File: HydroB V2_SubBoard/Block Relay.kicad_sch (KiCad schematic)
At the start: 25 parts, among them J14 Screw_Terminal_01x02, J15 Screw_Terminal_01x02, J16 Screw_Terminal_01x02, J17 Screw_Terminal_01x02, J18 Screw_Terminal_01x02, K10 SRD-05VDC-SL-C, K5 SRD-05VDC-SL-C, K7 SRD-05VDC-SL-C, K8 SRD-05VDC-SL-C, K9 SRD-05VDC-SL-C, Q10 S8050, Q6 S8050, Q7 S8050, Q8 S8050, Q9 S8050

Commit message: finish the subboard layout
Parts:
- J14, J15, J16, J17, J18: footprint Connector_Phoenix_MC:PhoenixContact_MC_1,5_2-G-3.5_1x02_P3.50mm_Horizontal -> Connector_Phoenix_MC:PhoenixContact_MC_1,5_2-G-3.81_1x02_P3.81mm_Horizontal
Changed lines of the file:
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@@
 			)
 		)
-		(property "Footprint" "Connector_Phoenix_MC:PhoenixContact_MC_1,5_2-G-3.5_1x02_P3.50mm_Horizontal"
+		(property "Footprint" "Connector_Phoenix_MC:PhoenixContact_MC_1,5_2-G-3.81_1x02_P3.81mm_Horizontal"
 			(at 172.72 58.42 0)
 			(effects
@@
 			)
 		)
-		(property "Footprint" "Connector_Phoenix_MC:PhoenixContact_MC_1,5_2-G-3.5_1x02_P3.50mm_Horizontal"
+		(property "Footprint" "Connector_Phoenix_MC:PhoenixContact_MC_1,5_2-G-3.81_1x02_P3.81mm_Horizontal"
 			(at 236.22 58.42 0)
 			(effects
@@
 			)
 		)
-		(property "Footprint" "Connector_Phoenix_MC:PhoenixContact_MC_1,5_2-G-3.5_1x02_P3.50mm_Horizontal"
+		(property "Footprint" "Connector_Phoenix_MC:PhoenixContact_MC_1,5_2-G-3.81_1x02_P3.81mm_Horizontal"
 			(at 101.6 58.42 0)
 			(effects
@@
 			)
 		)
-		(property "Footprint" "Connector_Phoenix_MC:PhoenixContact_MC_1,5_2-G-3.5_1x02_P3.50mm_Horizontal"
+		(property "Footprint" "Connector_Phoenix_MC:PhoenixContact_MC_1,5_2-G-3.81_1x02_P3.81mm_Horizontal"
 			(at 129.54 111.76 0)
 			(effects
@@
 			)
 		)
-		(property "Footprint" "Connector_Phoenix_MC:PhoenixContact_MC_1,5_2-G-3.5_1x02_P3.50mm_Horizontal"
+		(property "Footprint" "Connector_Phoenix_MC:PhoenixContact_MC_1,5_2-G-3.81_1x02_P3.81mm_Horizontal"
 			(at 215.9 111.76 0)
 			(effects

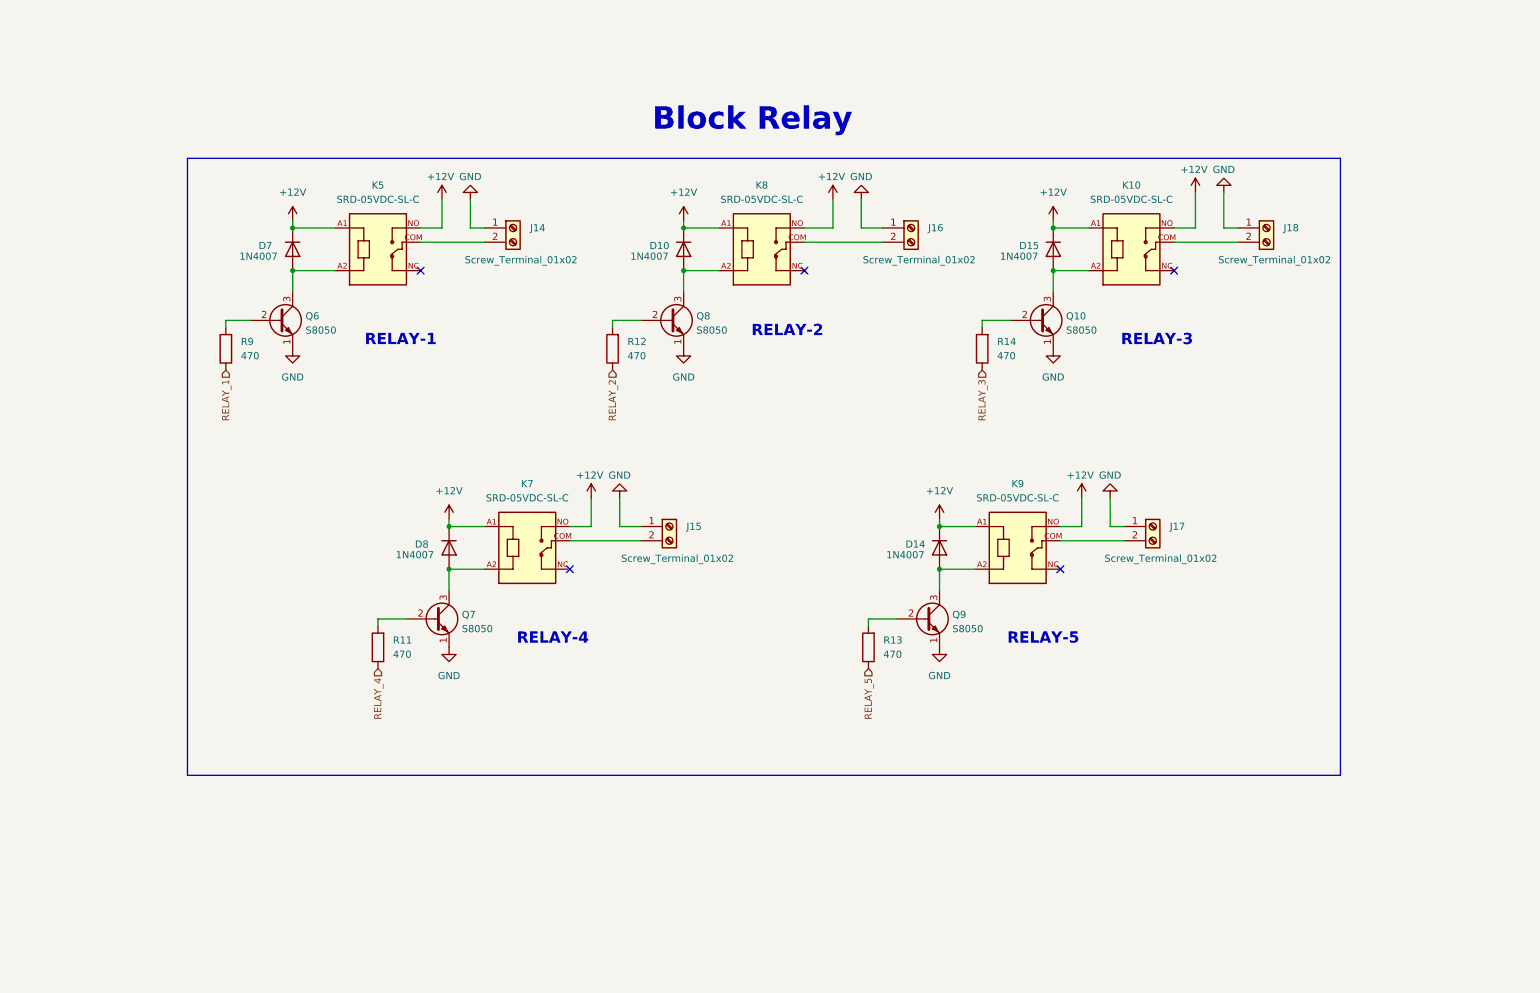
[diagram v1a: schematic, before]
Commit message: subboard updated for PCB placement
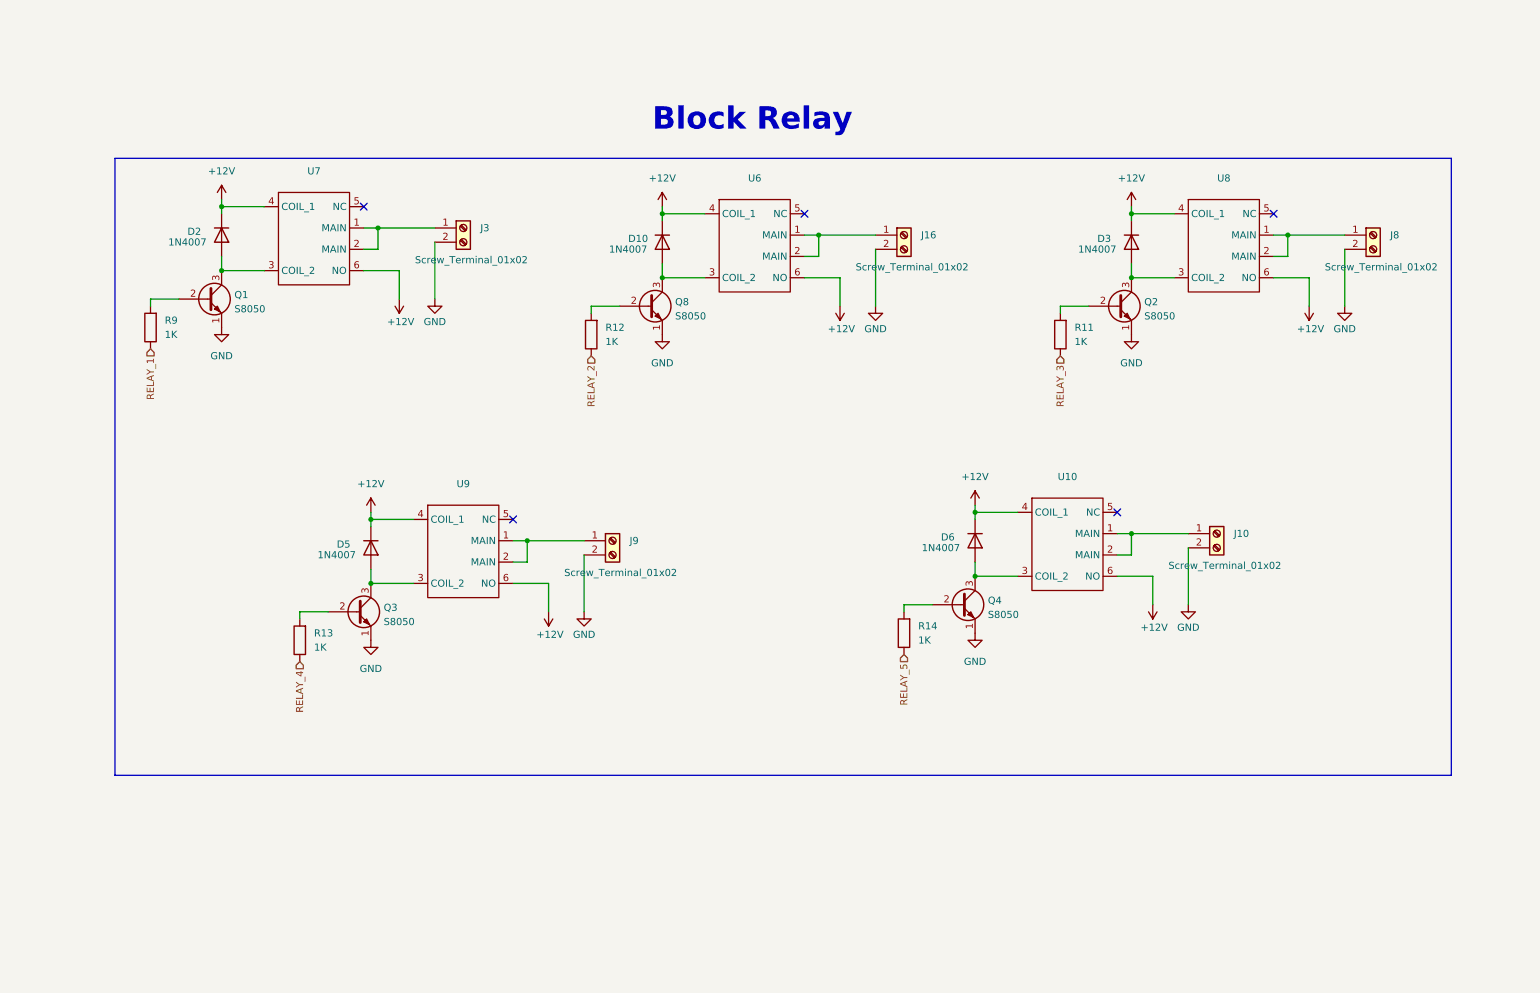
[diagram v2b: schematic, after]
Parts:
- removed D14, D15, D7, D8: 1N4007, Diode_SMD:D_SMA, symbol Diode:LL4148
- removed J14, J15, J17, J18: Screw_Terminal_01x02, Connector_Phoenix_MC:PhoenixContact_MC_1,5_2-G-3.81_1x02_P3.81mm_Horizontal, symbol Connector:Screw_Terminal_01x02
- removed K10, K5, K7, K8, K9: SRD-05VDC-SL-C, SRD-05VDC-SL-C (1):RELAY_SRD-05VDC-SL-C, symbol SRD-05VDC-SL-C:SRD-05VDC-SL-C
- removed Q10, Q6, Q7, Q9: S8050, Package_TO_SOT_SMD:SOT-23, symbol Transistor_BJT:S8050
- added D2, D3, D5, D6: 1N4007, Diode_SMD:D_SMA, symbol Diode:LL4148
- added J10, J3, J8, J9: Screw_Terminal_01x02, TerminalBlock_Phoenix:TerminalBlock_Phoenix_MKDS-1,5-2_1x02_P5.00mm_Horizontal, symbol Connector:Screw_Terminal_01x02
- added Q1, Q2, Q3, Q4: S8050, Package_TO_SOT_SMD:SOT-23, symbol Transistor_BJT:S8050
- added U10, U6, U7, U8, U9: ~, relay 12vdc 3A:RELAY-TH_SRS-12VDC-SL, symbol RELAY-12V-3A:RELAY-12V-3A
- J16: footprint Connector_Phoenix_MC:PhoenixContact_MC_1,5_2-G-3.81_1x02_P3.81mm_Horizontal -> TerminalBlock_Phoenix:TerminalBlock_Phoenix_MKDS-1,5-2_1x02_P5.00mm_Horizontal
- R11, R12, R13, R14, R9: value 470 -> 1K
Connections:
- net +12V: now also D2.1 (K), D3.1 (K), D5.1 (K), D6.1 (K), U10.4 (COIL_1), U10.6 (NO), U6.4 (COIL_1), U6.6 (NO), U7.4 (COIL_1), U7.6 (NO), U8.4 (COIL_1), U8.6 (NO), U9.4 (COIL_1), U9.6 (NO)
- net GND: now also J16.2 (Pin_2), J10.2 (Pin_2), J3.2 (Pin_2), J8.2 (Pin_2), J9.2 (Pin_2), Q1.1 (E), Q2.1 (E), Q3.1 (E), Q4.1 (E); no longer J16.1 (Pin_1)
- net RELAY_3: now also R11.1; no longer R14.1
- net RELAY_4: now also R13.1; no longer R11.1
- net RELAY_5: now also R14.1; no longer R13.1
- net at R11.2: now also Q2.2 (B)
- net at R14.2: now also Q4.2 (B)
- net at R13.2: now also Q3.2 (B)
- net at R9.2: now also Q1.2 (B)
- net at D10.2 (A), Q8.3 (C): now also U6.3 (COIL_2)
- new net: D6.2 (A), Q4.3 (C), U10.3 (COIL_2)
- new net: D3.2 (A), Q2.3 (C), U8.3 (COIL_2)
- new net: J10.1 (Pin_1), U10.1 (MAIN), U10.2 (MAIN)
- new net: J8.1 (Pin_1), U8.1 (MAIN), U8.2 (MAIN)
- new net: D5.2 (A), Q3.3 (C), U9.3 (COIL_2)
- new net: J16.1 (Pin_1), U6.1 (MAIN), U6.2 (MAIN)
- new net: D2.2 (A), Q1.3 (C), U7.3 (COIL_2)
- new net: J9.1 (Pin_1), U9.1 (MAIN), U9.2 (MAIN)
- new net: J3.1 (Pin_1), U7.1 (MAIN), U7.2 (MAIN)
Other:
- note removed: "RELAY-1"
- note removed: "RELAY-2"
- note removed: "RELAY-3"
- note removed: "RELAY-4"
- note removed: "RELAY-5"
- moved on the sheet: D10, J16, Q8, R12

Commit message: Subboard updated
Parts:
- added R18, R2, R22, R23, R3: 10K, Resistor_SMD:R_0603_1608Metric, symbol Device:R
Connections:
- net GND: now also R18.1, R2.1, R22.1, R23.1, R3.1
- net at Q4.2 (B), R14.2: now also R23.2
- net at Q3.2 (B), R13.2: now also R22.2
- net at Q2.2 (B), R11.2: now also R2.2
- net at Q1.2 (B), R9.2: now also R18.2
- net at Q8.2 (B), R12.2: now also R3.2
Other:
- moved on the sheet: R11, R12, R13, R14, R9

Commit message: subboard new update version
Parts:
- removed Q8: S8050, Package_TO_SOT_SMD:SOT-23, symbol Transistor_BJT:S8050
- added D11, D12, D13, D14, D9: LED, LED_SMD:LED_0603_1608Metric, symbol Device:LED
- added Q5: S8050, Package_TO_SOT_SMD:SOT-23, symbol Transistor_BJT:S8050
- added R24, R25, R26, R27, R28: 1K, Resistor_SMD:R_0603_1608Metric, symbol Device:R
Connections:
- net GND: now also Q1.2 (E), Q2.2 (E), Q3.2 (E), Q4.2 (E), Q5.2 (E); no longer Q1.1 (E), Q2.1 (E), Q3.1 (E), Q4.1 (E)
- net at R14.2, R23.2: now also Q4.1 (B); no longer Q4.2 (B)
- net at D6.2 (A), Q4.3 (C), U10.3 (COIL_2): now also D14.2 (A)
- net at D3.2 (A), Q2.3 (C), U8.3 (COIL_2): now also D12.2 (A)
- net at R13.2, R22.2: now also Q3.1 (B); no longer Q3.2 (B)
- net at D5.2 (A), Q3.3 (C), U9.3 (COIL_2): now also D13.2 (A)
- net at R11.2, R2.2: now also Q2.1 (B); no longer Q2.2 (B)
- net at R18.2, R9.2: now also Q1.1 (B); no longer Q1.2 (B)
- net at D2.2 (A), Q1.3 (C), U7.3 (COIL_2): now also D9.2 (A)
- net at R12.2, R3.2: now also Q5.1 (B)
- net at D10.2 (A), U6.3 (COIL_2): now also D11.2 (A), Q5.3 (C)
- new net: D13.1 (K), R27.2
- new net: D9.1 (K), R24.2
- new net: D11.1 (K), R25.2
- new net: D12.1 (K), R26.2
- new net: D14.1 (K), R28.2
- new net +3.3V: R24.1, R25.1, R26.1, R27.1, R28.1
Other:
- moved on the sheet: D2, J3, Q1, R11, R12, R13, R14, R18, R2, R22, R23, R3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

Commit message: PCB update
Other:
- moved on the sheet: D10, D11, D12, D13, D14, D2, D3, D5, D6, D9, J10, J16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

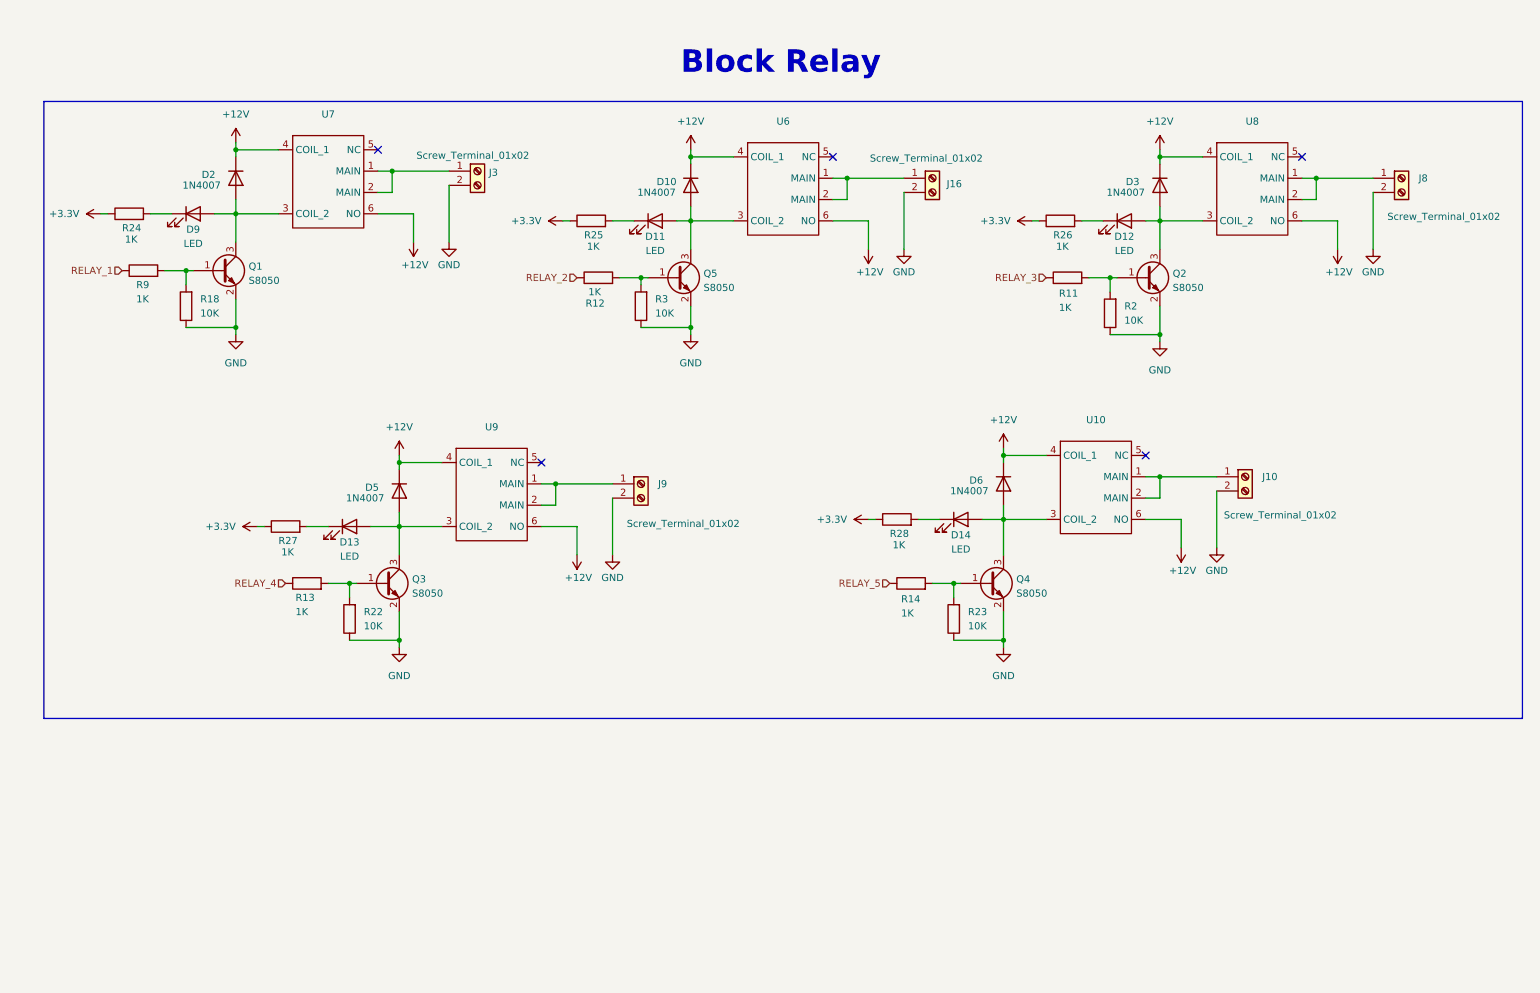
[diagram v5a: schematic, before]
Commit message: PCB component placement and layout
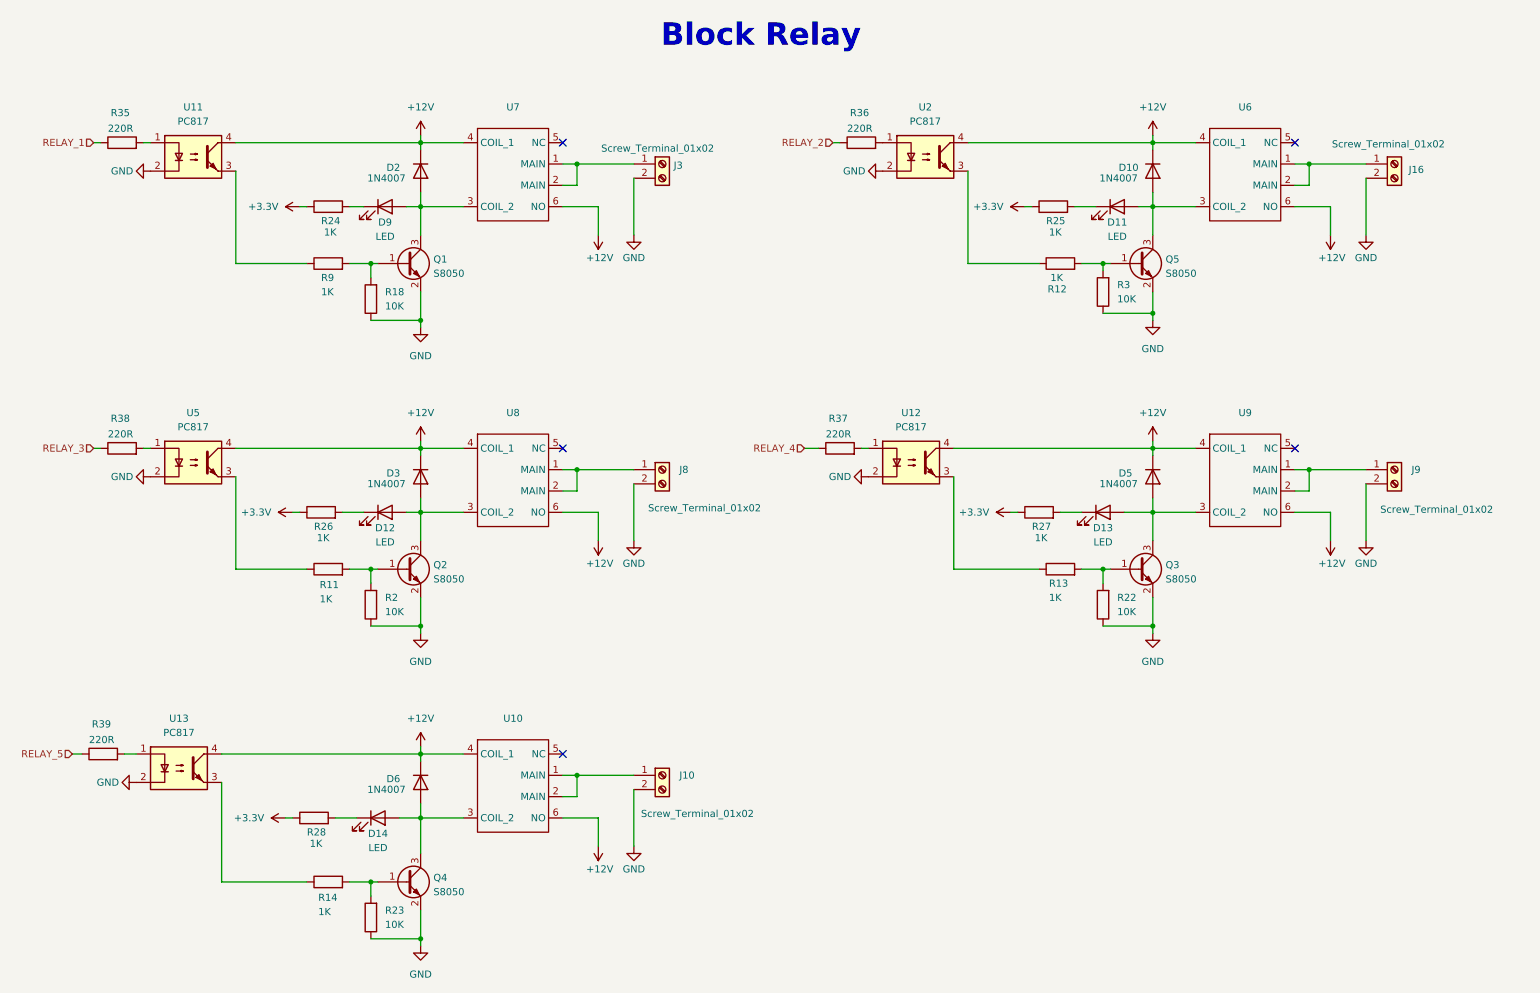
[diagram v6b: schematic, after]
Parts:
- added R35, R36, R37, R38, R39: 220R, Resistor_SMD:R_0603_1608Metric, symbol Device:R
- added U11, U12, U13, U2, U5: PC817, Package_DIP:DIP-4_W7.62mm_SMDSocket_SmallPads, symbol Isolator:PC817
- J10, J16, J3, J8, J9: footprint TerminalBlock_Phoenix:TerminalBlock_Phoenix_MKDS-1,5-2_1x02_P5.00mm_Horizontal -> Connector_JST:JST_EH_B2B-EH-A_1x02_P2.50mm_Vertical
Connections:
- net +12V: now also U11.4, U12.4, U13.4, U2.4, U5.4
- net GND: now also U11.2, U12.2, U13.2, U2.2, U5.2
- net RELAY_1: now also R35.1; no longer R9.1
- net RELAY_2: now also R36.1; no longer R12.1
- net RELAY_3: now also R38.1; no longer R11.1
- net RELAY_4: now also R37.1; no longer R13.1
- net RELAY_5: now also R39.1; no longer R14.1
- new net: R35.2, U11.1
- new net: R38.2, U5.1
- new net: R11.1, U5.3
- new net: R36.2, U2.1
- new net: R12.1, U2.3
- new net: R9.1, U11.3
- new net: R39.2, U13.1
- new net: R14.1, U13.3
- new net: R37.2, U12.1
- new net: R13.1, U12.3
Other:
- moved on the sheet: D10, D11, D12, D13, D14, D2, D3, D5, D6, D9, J10, J16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
